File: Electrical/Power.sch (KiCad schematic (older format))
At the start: 7 parts

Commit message: Small changes...
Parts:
- added C? (x2): 10uF, symbol C
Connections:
- net +BATT: now also C?.1, C?.1
- net GND: now also C?.2, C?.2
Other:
- moved on the sheet: C?, U?

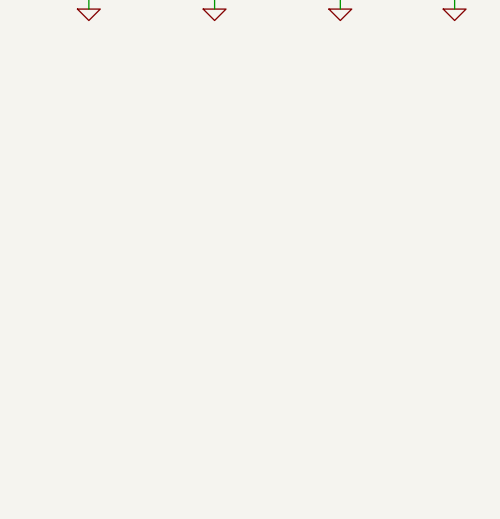
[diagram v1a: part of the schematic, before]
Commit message: Added voltage references and test points
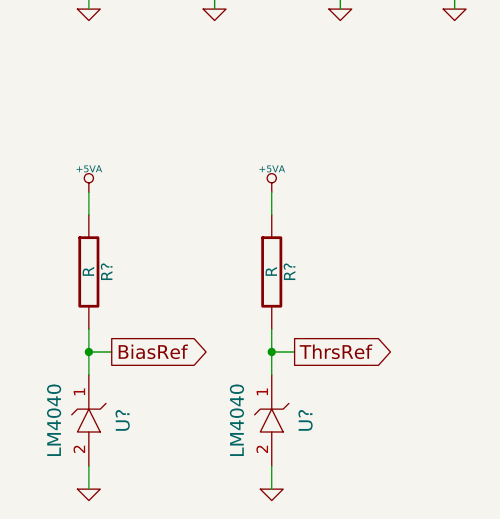
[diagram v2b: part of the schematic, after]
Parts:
- added R? (x2): R, symbol R
- added U? (x2): LM4040, symbol LM4040
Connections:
- net +5VA: now also R?.1, R?.1
- net GND: now also U?.2, U?.2
- new net BiasRef: R?.2, U?.1
- new net ThrsRef: R?.2, U?.1
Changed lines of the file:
@@
-EESchema Schematic File Version 2  date 4/17/2013 7:49:12 PM
+EESchema Schematic File Version 2  date 4/18/2013 6:48:03 PM
 LIBS:power
 LIBS:device
@@
 $Descr A4 11700 8267
 encoding utf-8
-Sheet 2 6
+Sheet 3 6
 Title "Cosmic Ray Detector"
-Date "17 apr 2013"
+Date "18 apr 2013"
 Rev "1A"
 Comp "Ethan Harstad"
@@
 Comment4 ""
 $EndDescr
+$Comp
+L LM4040 U?
+U 1 1 517085AF
+P 1900 6800
+F 0 "U?" H 1900 6950 60  0000 C CNN
+F 1 "LM4040" H 1900 6650 60  0000 C CNN
+	1    1900 6800
+	0    1    1    0
+$EndComp
+$Comp
+L R R?
+U 1 1 517085AE
+P 1900 6150
+F 0 "R?" V 1980 6150 50  0000 C CNN
+F 1 "R" V 1900 6150 50  0000 C CNN
+	1    1900 6150
+	1    0    0    -1
+$EndComp
+$Comp
+L GND #PWR?
+U 1 1 517085AD
+P 1900 7100
+F 0 "#PWR?" H 1900 7100 30  0001 C CNN
+F 1 "GND" H 1900 7030 30  0001 C CNN
+	1    1900 7100
+	1    0    0    -1
+$EndComp
+Text GLabel 2000 6500 2    60   Output ~ 0
+ThrsRef
+Wire Wire Line
+	1900 7000 1900 7100
+Wire Wire Line
+	1900 6400 1900 6600
+Wire Wire Line
+	2000 6500 1900 6500
+Connection ~ 1900 6500
+Wire Wire Line
+	1900 5900 1900 5800
+$Comp
+L +5VA #PWR?
+U 1 1 517085AC
+P 1900 5800
+F 0 "#PWR?" H 1900 5930 20  0001 C CNN
+F 1 "+5VA" H 1900 5900 30  0000 C CNN
+	1    1900 5800
+	1    0    0    -1
+$EndComp
+$Comp
+L +5VA #PWR?
+U 1 1 517085A0
+P 1100 5800
+F 0 "#PWR?" H 1100 5930 20  0001 C CNN
+F 1 "+5VA" H 1100 5900 30  0000 C CNN
+	1    1100 5800
+	1    0    0    -1
+$EndComp
+Wire Wire Line
+	1100 5900 1100 5800
+Connection ~ 1100 6500
+Wire Wire Line
+	1200 6500 1100 6500
 Wire Wire Line
 	1500 1600 1500 1700
@@
 Wire Wire Line
 	1100 1600 1100 1700
+Wire Wire Line
+	1100 6400 1100 6600
+Wire Wire Line
+	1100 7000 1100 7100
+Text GLabel 1200 6500 2    60   Output ~ 0
+BiasRef
+$Comp
+L GND #PWR?
+U 1 1 51708550
+P 1100 7100
+F 0 "#PWR?" H 1100 7100 30  0001 C CNN
+F 1 "GND" H 1100 7030 30  0001 C CNN
+	1    1100 7100
+	1    0    0    -1
+$EndComp
+$Comp
+L R R?
+U 1 1 51708537
+P 1100 6150
+F 0 "R?" V 1180 6150 50  0000 C CNN
+F 1 "R" V 1100 6150 50  0000 C CNN
+	1    1100 6150
+	1    0    0    -1
+$EndComp
+$Comp
+L LM4040 U?
+U 1 1 51708532
+P 1100 6800
+F 0 "U?" H 1100 6950 60  0000 C CNN
+F 1 "LM4040" H 1100 6650 60  0000 C CNN
+	1    1100 6800
+	0    1    1    0
+$EndComp
 $Comp
 L +BATT #PWR?

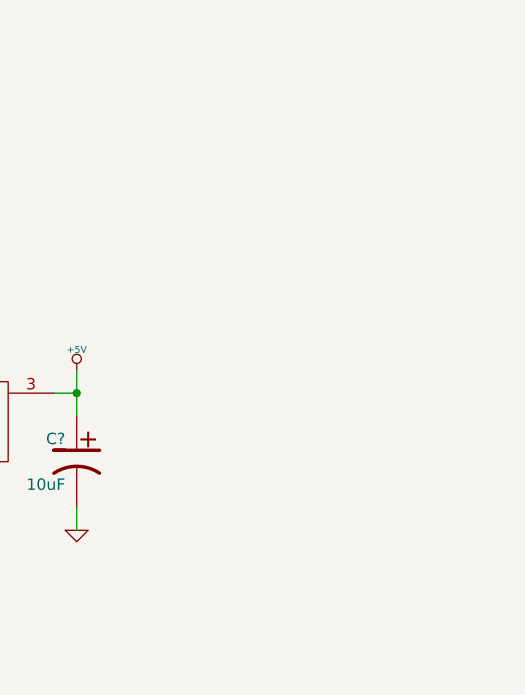
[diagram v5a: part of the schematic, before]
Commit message: Added sensors/data logger with ChipKit Max
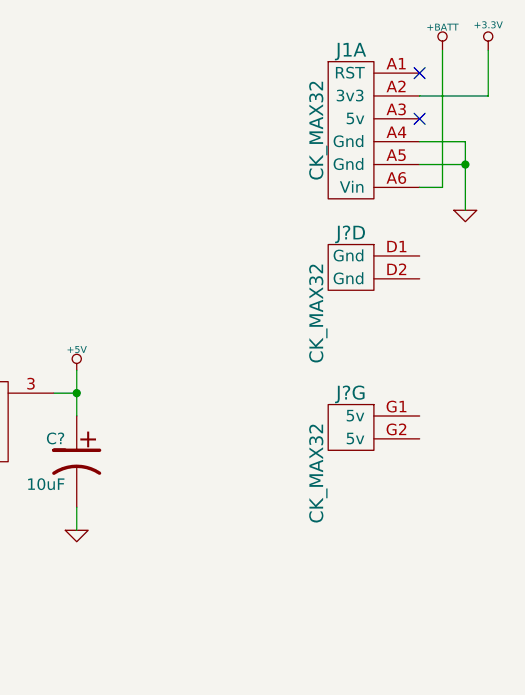
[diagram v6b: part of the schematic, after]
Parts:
- added J1, J? (x2): CK_MAX32, symbol CK_MAX32
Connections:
- net +BATT: now also J1.A6 (Vin)
- net GND: now also J1.A4 (Gnd), J1.A5 (Gnd)
- new net +3.3V: J1.A2 (3v3)
- no-connect marks 0 -> 2
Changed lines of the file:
@@
-EESchema Schematic File Version 2  date 4/19/2013 7:14:36 PM
+EESchema Schematic File Version 2  date 5/4/2013 6:32:29 PM
 LIBS:power
 LIBS:device
@@
 $Descr A4 11700 8267
 encoding utf-8
-Sheet 3 6
+Sheet 3 7
 Title "Cosmic Ray Detector"
-Date "20 apr 2013"
+Date "4 may 2013"
 Rev "1A"
 Comp "Ethan Harstad"
@@
 Comment4 ""
 $EndDescr
+NoConn ~ 3800 1300
+Connection ~ 4000 1500
+Wire Wire Line
+	4000 1700 4000 1400
+Wire Wire Line
+	4000 1400 3800 1400
+Wire Wire Line
+	3800 1200 4100 1200
+Wire Wire Line
+	4100 1200 4100 1000
+Wire Wire Line
+	1900 7000 1900 7100
+Wire Wire Line
+	1900 6400 1900 6600
+Wire Wire Line
+	2000 6500 1900 6500
+Connection ~ 1900 6500
+Wire Wire Line
+	1900 5900 1900 5800
+Wire Wire Line
+	1100 5900 1100 5800
+Connection ~ 1100 6500
+Wire Wire Line
+	1200 6500 1100 6500
+Wire Wire Line
+	1500 1600 1500 1700
+Connection ~ 1100 1100
+Wire Wire Line
+	1500 1200 1500 1100
+Wire Wire Line
+	1500 1100 1100 1100
+Wire Wire Line
+	2700 4800 2700 5000
+Wire Wire Line
+	1650 4750 1650 5000
+Connection ~ 1100 4400
+Wire Wire Line
+	1200 4400 1100 4400
+Wire Wire Line
+	1100 4200 1100 4500
+Wire Wire Line
+	2700 4200 2700 4400
+Wire Wire Line
+	1100 3000 1100 3100
+Wire Wire Line
+	1100 2600 1100 2400
+Wire Wire Line
+	2300 2600 2300 2400
+Wire Wire Line
+	1700 3100 1700 3000
+Wire Wire Line
+	2300 3100 2300 3000
+Wire Wire Line
+	2200 2500 2300 2500
+Connection ~ 2300 2500
+Wire Wire Line
+	1200 2500 1100 2500
+Connection ~ 1100 2500
+Wire Wire Line
+	2100 4400 2200 4400
+Wire Wire Line
+	2200 4400 2200 4500
+Wire Wire Line
+	2100 4300 2700 4300
+Connection ~ 2700 4300
+Wire Wire Line
+	1200 4300 1100 4300
+Connection ~ 1100 4300
+Wire Wire Line
+	1100 4900 1100 5000
+Wire Wire Line
+	2200 4900 2200 5000
+Wire Wire Line
+	1100 1000 1100 1200
+Wire Wire Line
+	1100 1600 1100 1700
+Wire Wire Line
+	1100 6400 1100 6600
+Wire Wire Line
+	1100 7000 1100 7100
+Wire Wire Line
+	3900 1000 3900 1600
+Wire Wire Line
+	3900 1600 3800 1600
+Wire Wire Line
+	4000 1500 3800 1500
+$Comp
+L GND #PWR?
+U 1 1 51858C8B
+P 4000 1700
+F 0 "#PWR?" H 4000 1700 30  0001 C CNN
+F 1 "GND" H 4000 1630 30  0001 C CNN
+	1    4000 1700
+	1    0    0    -1
+$EndComp
+NoConn ~ 3800 1100
+$Comp
+L +3.3V #PWR?
+U 1 1 51858C75
+P 4100 1000
+F 0 "#PWR?" H 4100 960 30  0001 C CNN
+F 1 "+3.3V" H 4100 1110 30  0000 C CNN
+	1    4100 1000
+	1    0    0    -1
+$EndComp
+$Comp
+L +BATT #PWR?
+U 1 1 51858C69
+P 3900 1000
+F 0 "#PWR?" H 3900 950 20  0001 C CNN
+F 1 "+BATT" H 3900 1100 30  0000 C CNN
+	1    3900 1000
+	1    0    0    -1
+$EndComp
+$Comp
+L CK_MAX32 J?
+U 7 1 51858A2F
+P 3500 2600
+F 0 "J?" H 3500 2700 60  0000 C CNN
+F 1 "CK_MAX32" V 3350 2350 60  0000 C CNN
+	7    3500 2600
+	1    0    0    -1
+$EndComp
+$Comp
+L CK_MAX32 J?
+U 4 1 51858A27
+P 3500 1900
+F 0 "J?" H 3500 2000 60  0000 C CNN
+F 1 "CK_MAX32" V 3350 1650 60  0000 C CNN
+	4    3500 1900
+	1    0    0    -1
+$EndComp
+$Comp
+L CK_MAX32 J1
+U 1 1 518589A7
+P 3500 1100
+F 0 "J1" H 3500 1200 60  0000 C CNN
+F 1 "CK_MAX32" V 3350 850 60  0000 C CNN
+	1    3500 1100
+	1    0    0    -1
+$EndComp
 $Comp
 L LM4040 U?
@@
 Text GLabel 2000 6500 2    60   Output ~ 0
 ThrsRef
-Wire Wire Line
-	1900 7000 1900 7100
-Wire Wire Line
-	1900 6400 1900 6600
-Wire Wire Line
-	2000 6500 1900 6500
-Connection ~ 1900 6500
-Wire Wire Line
-	1900 5900 1900 5800
 $Comp
 L +5VA #PWR?
@@
 	1    0    0    -1
 $EndComp
-Wire Wire Line
-	1100 5900 1100 5800
-Connection ~ 1100 6500
-Wire Wire Line
-	1200 6500 1100 6500
-Wire Wire Line
-	1500 1600 1500 1700
-Connection ~ 1100 1100
-Wire Wire Line
-	1500 1200 1500 1100
-Wire Wire Line
-	1500 1100 1100 1100
-Wire Wire Line
-	2700 4800 2700 5000
-Wire Wire Line
-	1650 4750 1650 5000
-Connection ~ 1100 4400
-Wire Wire Line
-	1200 4400 1100 4400
-Wire Wire Line
-	1100 4200 1100 4500
-Wire Wire Line
-	2700 4200 2700 4400
-Wire Wire Line
-	1100 3000 1100 3100
-Wire Wire Line
-	1100 2600 1100 2400
-Wire Wire Line
-	2300 2600 2300 2400
-Wire Wire Line
-	1700 3100 1700 3000
-Wire Wire Line
-	2300 3100 2300 3000
-Wire Wire Line
-	2200 2500 2300 2500
-Connection ~ 2300 2500
-Wire Wire Line
-	1200 2500 1100 2500
-Connection ~ 1100 2500
-Wire Wire Line
-	2100 4400 2200 4400
-Wire Wire Line
-	2200 4400 2200 4500
-Wire Wire Line
-	2100 4300 2700 4300
-Connection ~ 2700 4300
-Wire Wire Line
-	1200 4300 1100 4300
-Connection ~ 1100 4300
-Wire Wire Line
-	1100 4900 1100 5000
-Wire Wire Line
-	2200 4900 2200 5000
-Wire Wire Line
-	1100 1000 1100 1200
-Wire Wire Line
-	1100 1600 1100 1700
-Wire Wire Line
-	1100 6400 1100 6600
-Wire Wire Line
-	1100 7000 1100 7100
 Text GLabel 1200 6500 2    60   Output ~ 0
 BiasRef

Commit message: Annotated schematic
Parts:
- C14: renamed from C?; Voltage (none) -> 10V
- C15: renamed from C?; ESR (none) -> 2Ω; Voltage (none) -> 10V
- gave numbers to parts that had none: 12
- renumbered J1 to J2
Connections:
- no-connect marks 2 -> 6
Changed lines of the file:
@@
-EESchema Schematic File Version 2  date 5/4/2013 6:32:29 PM
+EESchema Schematic File Version 2  date 5/5/2013 3:54:39 PM
 LIBS:power
 LIBS:device
@@
 Sheet 3 7
 Title "Cosmic Ray Detector"
-Date "4 may 2013"
+Date "5 may 2013"
 Rev "1A"
 Comp "Ethan Harstad"
@@
 Comment4 ""
 $EndDescr
+NoConn ~ 3800 2700
+NoConn ~ 3800 2600
+NoConn ~ 3800 2000
+NoConn ~ 3800 1900
 NoConn ~ 3800 1300
 Connection ~ 4000 1500
@@
 	4000 1500 3800 1500
 $Comp
-L GND #PWR?
+L GND #PWR45
 U 1 1 51858C8B
 P 4000 1700
-F 0 "#PWR?" H 4000 1700 30  0001 C CNN
+F 0 "#PWR45" H 4000 1700 30  0001 C CNN
 F 1 "GND" H 4000 1630 30  0001 C CNN
 	1    4000 1700
@@
 NoConn ~ 3800 1100
 $Comp
-L +3.3V #PWR?
+L +3.3V #PWR46
 U 1 1 51858C75
 P 4100 1000
-F 0 "#PWR?" H 4100 960 30  0001 C CNN
+F 0 "#PWR46" H 4100 960 30  0001 C CNN
 F 1 "+3.3V" H 4100 1110 30  0000 C CNN
 	1    4100 1000
@@
 $EndComp
 $Comp
-L +BATT #PWR?
+L +BATT #PWR44
 U 1 1 51858C69
 P 3900 1000
-F 0 "#PWR?" H 3900 950 20  0001 C CNN
+F 0 "#PWR44" H 3900 950 20  0001 C CNN
 F 1 "+BATT" H 3900 1100 30  0000 C CNN
 	1    3900 1000
@@
 $EndComp
 $Comp
-L CK_MAX32 J?
+L CK_MAX32 J2
 U 7 1 51858A2F
 P 3500 2600
-F 0 "J?" H 3500 2700 60  0000 C CNN
+F 0 "J2" H 3500 2700 60  0000 C CNN
 F 1 "CK_MAX32" V 3350 2350 60  0000 C CNN
 	7    3500 2600
@@
 $EndComp
 $Comp
-L CK_MAX32 J?
+L CK_MAX32 J2
 U 4 1 51858A27
 P 3500 1900
-F 0 "J?" H 3500 2000 60  0000 C CNN
+F 0 "J2" H 3500 2000 60  0000 C CNN
 F 1 "CK_MAX32" V 3350 1650 60  0000 C CNN
 	4    3500 1900
@@
 $EndComp
 $Comp
-L CK_MAX32 J1
+L CK_MAX32 J2
 U 1 1 518589A7
 P 3500 1100
-F 0 "J1" H 3500 1200 60  0000 C CNN
+F 0 "J2" H 3500 1200 60  0000 C CNN
 F 1 "CK_MAX32" V 3350 850 60  0000 C CNN
 	1    3500 1100
@@
 $EndComp
 $Comp
-L LM4040 U?
+L LM4040 U6
 U 1 1 517085AF
 P 1900 6800
-F 0 "U?" H 1900 6950 60  0000 C CNN
+F 0 "U6" H 1900 6950 60  0000 C CNN
 F 1 "LM4040" H 1900 6650 60  0000 C CNN
 	1    1900 6800
@@
 $EndComp
 $Comp
-L R R?
+L R R7
 U 1 1 517085AE
 P 1900 6150
-F 0 "R?" V 1980 6150 50  0000 C CNN
+F 0 "R7" V 1980 6150 50  0000 C CNN
 F 1 "R" V 1900 6150 50  0000 C CNN
 	1    1900 6150
@@
 $EndComp
 $Comp
-L GND #PWR?
+L GND #PWR38
 U 1 1 517085AD
 P 1900 7100
-F 0 "#PWR?" H 1900 7100 30  0001 C CNN
+F 0 "#PWR38" H 1900 7100 30  0001 C CNN
 F 1 "GND" H 1900 7030 30  0001 C CNN
 	1    1900 7100
@@
 ThrsRef
 $Comp
-L +5VA #PWR?
+L +5VA #PWR37
 U 1 1 517085AC
 P 1900 5800
-F 0 "#PWR?" H 1900 5930 20  0001 C CNN
+F 0 "#PWR37" H 1900 5930 20  0001 C CNN
 F 1 "+5VA" H 1900 5900 30  0000 C CNN
 	1    1900 5800
@@
 $EndComp
 $Comp
-L +5VA #PWR?
+L +5VA #PWR32
 U 1 1 517085A0
 P 1100 5800
-F 0 "#PWR?" H 1100 5930 20  0001 C CNN
+F 0 "#PWR32" H 1100 5930 20  0001 C CNN
 F 1 "+5VA" H 1100 5900 30  0000 C CNN
 	1    1100 5800
@@
 BiasRef
 $Comp
-L GND #PWR?
+L GND #PWR33
 U 1 1 51708550
 P 1100 7100
-F 0 "#PWR?" H 1100 7100 30  0001 C CNN
+F 0 "#PWR33" H 1100 7100 30  0001 C CNN
 F 1 "GND" H 1100 7030 30  0001 C CNN
 	1    1100 7100
@@
 $EndComp
 $Comp
-L R R?
+L R R6
 U 1 1 51708537
 P 1100 6150
-F 0 "R?" V 1180 6150 50  0000 C CNN
+F 0 "R6" V 1180 6150 50  0000 C CNN
 F 1 "R" V 1100 6150 50  0000 C CNN
 	1    1100 6150
@@
 $EndComp
 $Comp
-L LM4040 U?
+L LM4040 U3
 U 1 1 51708532
 P 1100 6800
-F 0 "U?" H 1100 6950 60  0000 C CNN
+F 0 "U3" H 1100 6950 60  0000 C CNN
 F 1 "LM4040" H 1100 6650 60  0000 C CNN
 	1    1100 6800
@@
 $EndComp
 $Comp
-L +BATT #PWR?
+L +BATT #PWR26
 U 1 1 516DF49D
 P 1100 1000
-F 0 "#PWR?" H 1100 950 20  0001 C CNN
+F 0 "#PWR26" H 1100 950 20  0001 C CNN
 F 1 "+BATT" H 1100 1100 30  0000 C CNN
 	1    1100 1000
@@
 $EndComp
 $Comp
-L GND #PWR?
+L GND #PWR34
 U 1 1 516DF494
 P 1500 1700
-F 0 "#PWR?" H 1500 1700 30  0001 C CNN
+F 0 "#PWR34" H 1500 1700 30  0001 C CNN
 F 1 "GND" H 1500 1630 30  0001 C CNN
 	1    1500 1700
@@
 $EndComp
 $Comp
-L GND #PWR?
+L GND #PWR27
 U 1 1 516DF491
 P 1100 1700
-F 0 "#PWR?" H 1100 1700 30  0001 C CNN
+F 0 "#PWR27" H 1100 1700 30  0001 C CNN
 F 1 "GND" H 1100 1630 30  0001 C CNN
 	1    1100 1700
@@
 $EndComp
 $Comp
-L C C?
+L C C12
 U 1 1 516DF48A
 P 1500 1400
-F 0 "C?" H 1550 1500 50  0000 L CNN
+F 0 "C12" H 1550 1500 50  0000 L CNN
 F 1 "10uF" H 1550 1300 50  0000 L CNN
 	1    1500 1400
@@
 $EndComp
 $Comp
-L C C?
+L C C9
 U 1 1 516DF480
 P 1100 1400
-F 0 "C?" H 1150 1500 50  0000 L CNN
+F 0 "C9" H 1150 1500 50  0000 L CNN
 F 1 "10uF" H 1150 1300 50  0000 L CNN
 	1    1100 1400
@@
 $EndComp
 $Comp
-L +BATT #PWR?
+L +BATT #PWR30
 U 1 1 516CB878
 P 1100 4200
-F 0 "#PWR?" H 1100 4150 20  0001 C CNN
+F 0 "#PWR30" H 1100 4150 20  0001 C CNN
 F 1 "+BATT" H 1100 4300 30  0000 C CNN
 	1    1100 4200
@@
 $EndComp
 $Comp
-L GND #PWR?
+L GND #PWR43
 U 1 1 516CB872
 P 2700 5000
-F 0 "#PWR?" H 2700 5000 30  0001 C CNN
+F 0 "#PWR43" H 2700 5000 30  0001 C CNN
 F 1 "GND" H 2700 4930 30  0001 C CNN
 	1    2700 5000
@@
 $EndComp
 $Comp
-L GND #PWR?
+L GND #PWR39
 U 1 1 516CB870
 P 2200 5000
-F 0 "#PWR?" H 2200 5000 30  0001 C CNN
+F 0 "#PWR39" H 2200 5000 30  0001 C CNN
 F 1 "GND" H 2200 4930 30  0001 C CNN
 	1    2200 5000
@@
 $EndComp
 $Comp
-L GND #PWR?
+L GND #PWR35
 U 1 1 516CB86D
 P 1650 5000
-F 0 "#PWR?" H 1650 5000 30  0001 C CNN
+F 0 "#PWR35" H 1650 5000 30  0001 C CNN
 F 1 "GND" H 1650 4930 30  0001 C CNN
 	1    1650 5000
@@
 $EndComp
 $Comp
-L GND #PWR?
+L GND #PWR31
 U 1 1 516CB86A
 P 1100 5000
-F 0 "#PWR?" H 1100 5000 30  0001 C CNN
+F 0 "#PWR31" H 1100 5000 30  0001 C CNN
 F 1 "GND" H 1100 4930 30  0001 C CNN
 	1    1100 5000
@@
 $EndComp
 $Comp
-L C C?
+L C C11
 U 1 1 516CB860
 P 1100 4700
-F 0 "C?" H 1150 4800 50  0000 L CNN
+F 0 "C11" H 1150 4800 50  0000 L CNN
 F 1 "0.1uF" H 1150 4600 50  0000 L CNN
 	1    1100 4700
@@
 $EndComp
 $Comp
-L +5VA #PWR?
+L +5VA #PWR42
 U 1 1 516CB84D
 P 2700 4200
-F 0 "#PWR?" H 2700 4330 20  0001 C CNN
+F 0 "#PWR42" H 2700 4330 20  0001 C CNN
 F 1 "+5VA" H 2700 4300 30  0000 C CNN
 	1    2700 4200
@@
 $EndComp
 $Comp
-L CP1 C?
+L CP1 C15
 U 1 1 516CB82C
 P 2700 4600
-F 0 "C?" H 2750 4700 50  0000 L CNN
+F 0 "C15" H 2750 4700 50  0000 L CNN
 F 1 "2.2uF" H 2750 4500 50  0000 L CNN
+F 4 "10V" H 2650 4500 60  0000 R CNN "Voltage"
+F 5 "2Ω" H 2600 4700 60  0000 R CNN "ESR"
 	1    2700 4600
 	-1   0    0    -1
 $EndComp
 $Comp
-L C C?
+L C C13
 U 1 1 516CB80A
 P 2200 4700
-F 0 "C?" H 2250 4800 50  0000 L CNN
+F 0 "C13" H 2250 4800 50  0000 L CNN
 F 1 "470pF" H 2250 4600 50  0000 L CNN
 	1    2200 4700
@@
 $EndComp
 $Comp
-L MIC5219 U?
+L MIC5219 U4
 U 1 1 516CB804
 P 1650 4300
-F 0 "U?" H 1650 4300 60  0000 C CNN
+F 0 "U4" H 1650 4300 60  0000 C CNN
 F 1 "MIC5219-5" H 1650 4400 60  0000 C CNN
 	1    1650 4300
@@
 $EndComp
 $Comp
-L +BATT #PWR?
+L +BATT #PWR28
 U 1 1 516C8D2E
 P 1100 2400
-F 0 "#PWR?" H 1100 2350 20  0001 C CNN
+F 0 "#PWR28" H 1100 2350 20  0001 C CNN
 F 1 "+BATT" H 1100 2500 30  0000 C CNN
 	1    1100 2400
@@
 $EndComp
 $Comp
-L +5V #PWR?
+L +5V #PWR40
 U 1 1 516C8D22
 P 2300 2400
-F 0 "#PWR?" H 2300 2490 20  0001 C CNN
+F 0 "#PWR40" H 2300 2490 20  0001 C CNN
 F 1 "+5V" H 2300 2490 30  0000 C CNN
 	1    2300 2400
@@
 $EndComp
 $Comp
-L GND #PWR?
+L GND #PWR41
 U 1 1 516C8D19
 P 2300 3100
-F 0 "#PWR?" H 2300 3100 30  0001 C CNN
+F 0 "#PWR41" H 2300 3100 30  0001 C CNN
 F 1 "GND" H 2300 3030 30  0001 C CNN
 	1    2300 3100
@@
 $EndComp
 $Comp
-L GND #PWR?
+L GND #PWR29
 U 1 1 516C8D14
 P 1100 3100
-F 0 "#PWR?" H 1100 3100 30  0001 C CNN
+F 0 "#PWR29" H 1100 3100 30  0001 C CNN
 F 1 "GND" H 1100 3030 30  0001 C CNN
 	1    1100 3100
@@
 $EndComp
 $Comp
-L GND #PWR?
+L GND #PWR36
 U 1 1 516C8D0D
 P 1700 3100
-F 0 "#PWR?" H 1700 3100 30  0001 C CNN
+F 0 "#PWR36" H 1700 3100 30  0001 C CNN
 F 1 "GND" H 1700 3030 30  0001 C CNN
 	1    1700 3100
@@
 $EndComp
 $Comp
-L C C?
+L C C10
 U 1 1 516C8D02
 P 1100 2800
-F 0 "C?" H 1150 2900 50  0000 L CNN
+F 0 "C10" H 1150 2900 50  0000 L CNN
 F 1 "0.1uF" H 1150 2700 50  0000 L CNN
 	1    1100 2800
@@
 $EndComp
 $Comp
-L CP1 C?
+L CP1 C14
 U 1 1 516C8CB0
 P 2300 2800
-F 0 "C?" H 2350 2900 50  0000 L CNN
+F 0 "C14" H 2350 2900 50  0000 L CNN
 F 1 "10uF" H 2350 2700 50  0000 L CNN
+F 4 "10V" H 2250 2700 60  0000 R CNN "Voltage"
 	1    2300 2800
 	-1   0    0    -1
 $EndComp
 $Comp
-L REG_3 U?
+L REG_3 U5
 U 1 1 516C8C9B
 P 1700 2500
-F 0 "U?" H 1700 2500 60  0000 C CNN
+F 0 "U5" H 1700 2500 60  0000 C CNN
 F 1 "MIC29300-5" H 1700 2600 60  0000 C CNN
 	1    1700 2500
